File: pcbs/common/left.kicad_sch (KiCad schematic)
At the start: 89 parts, among them J2 TRS

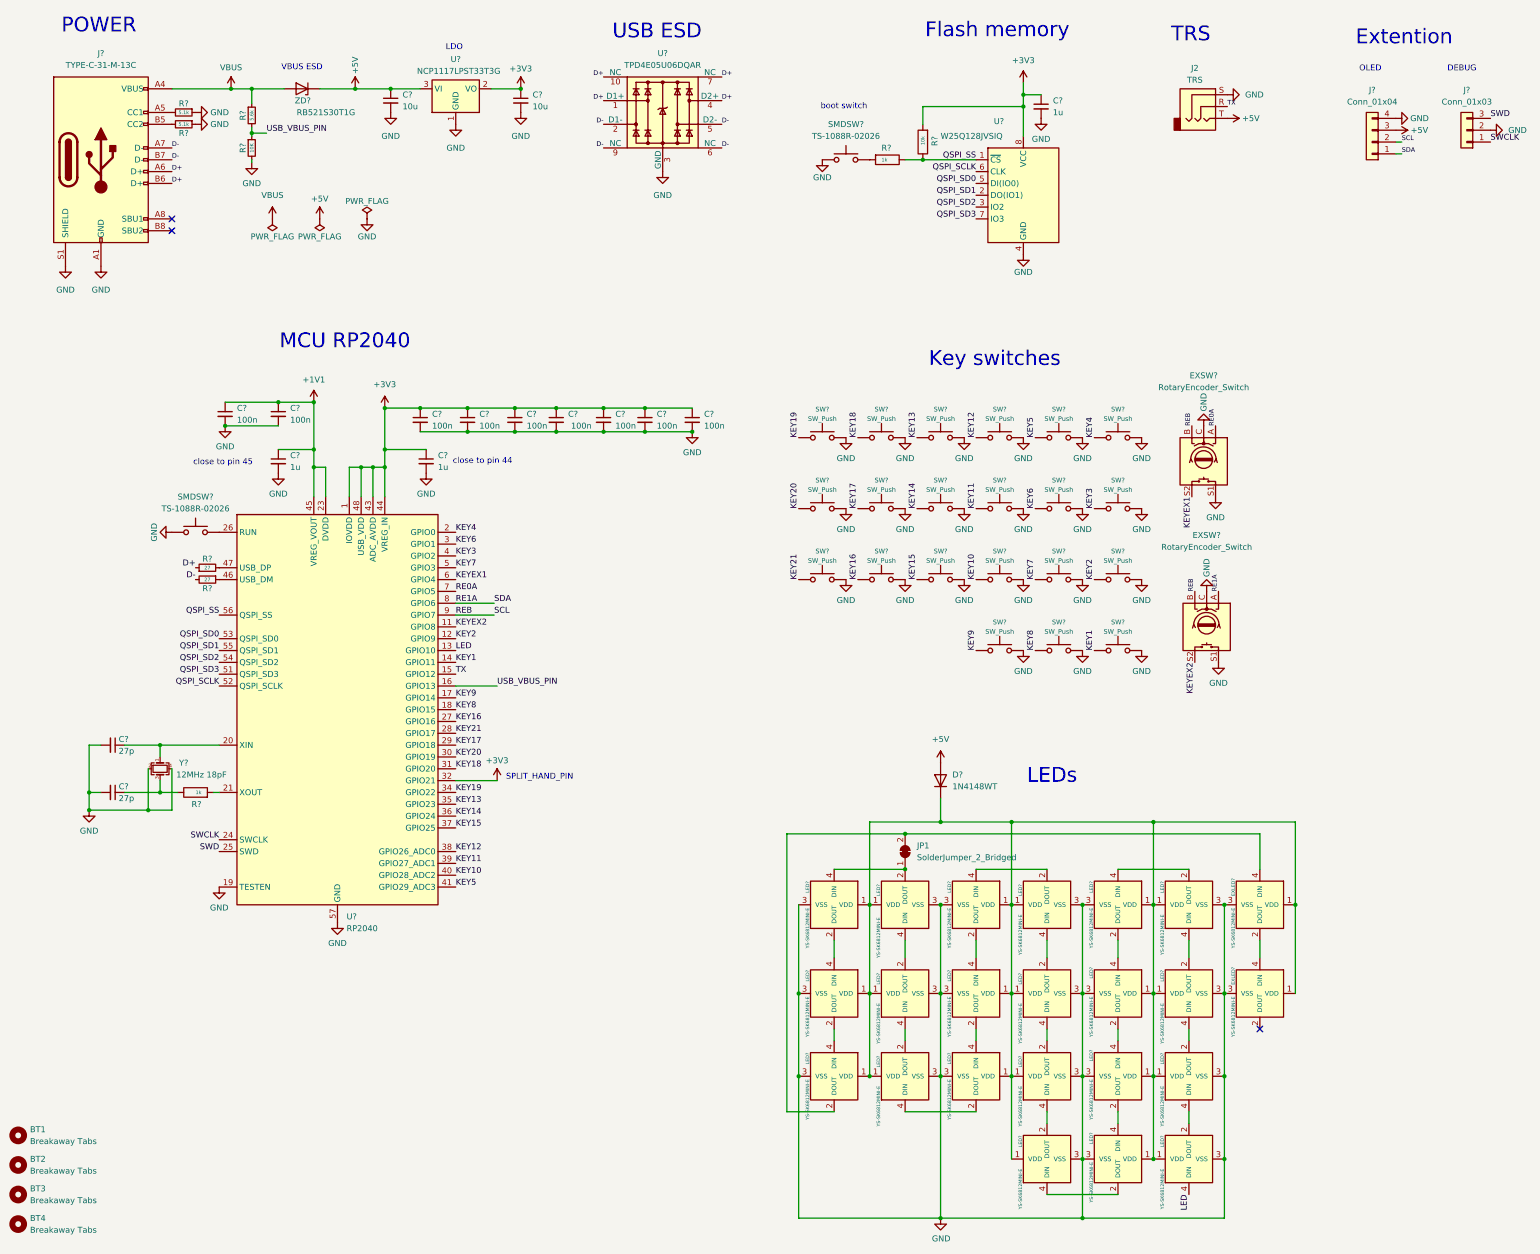
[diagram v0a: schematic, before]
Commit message: Add USB C port to replace TRS jack
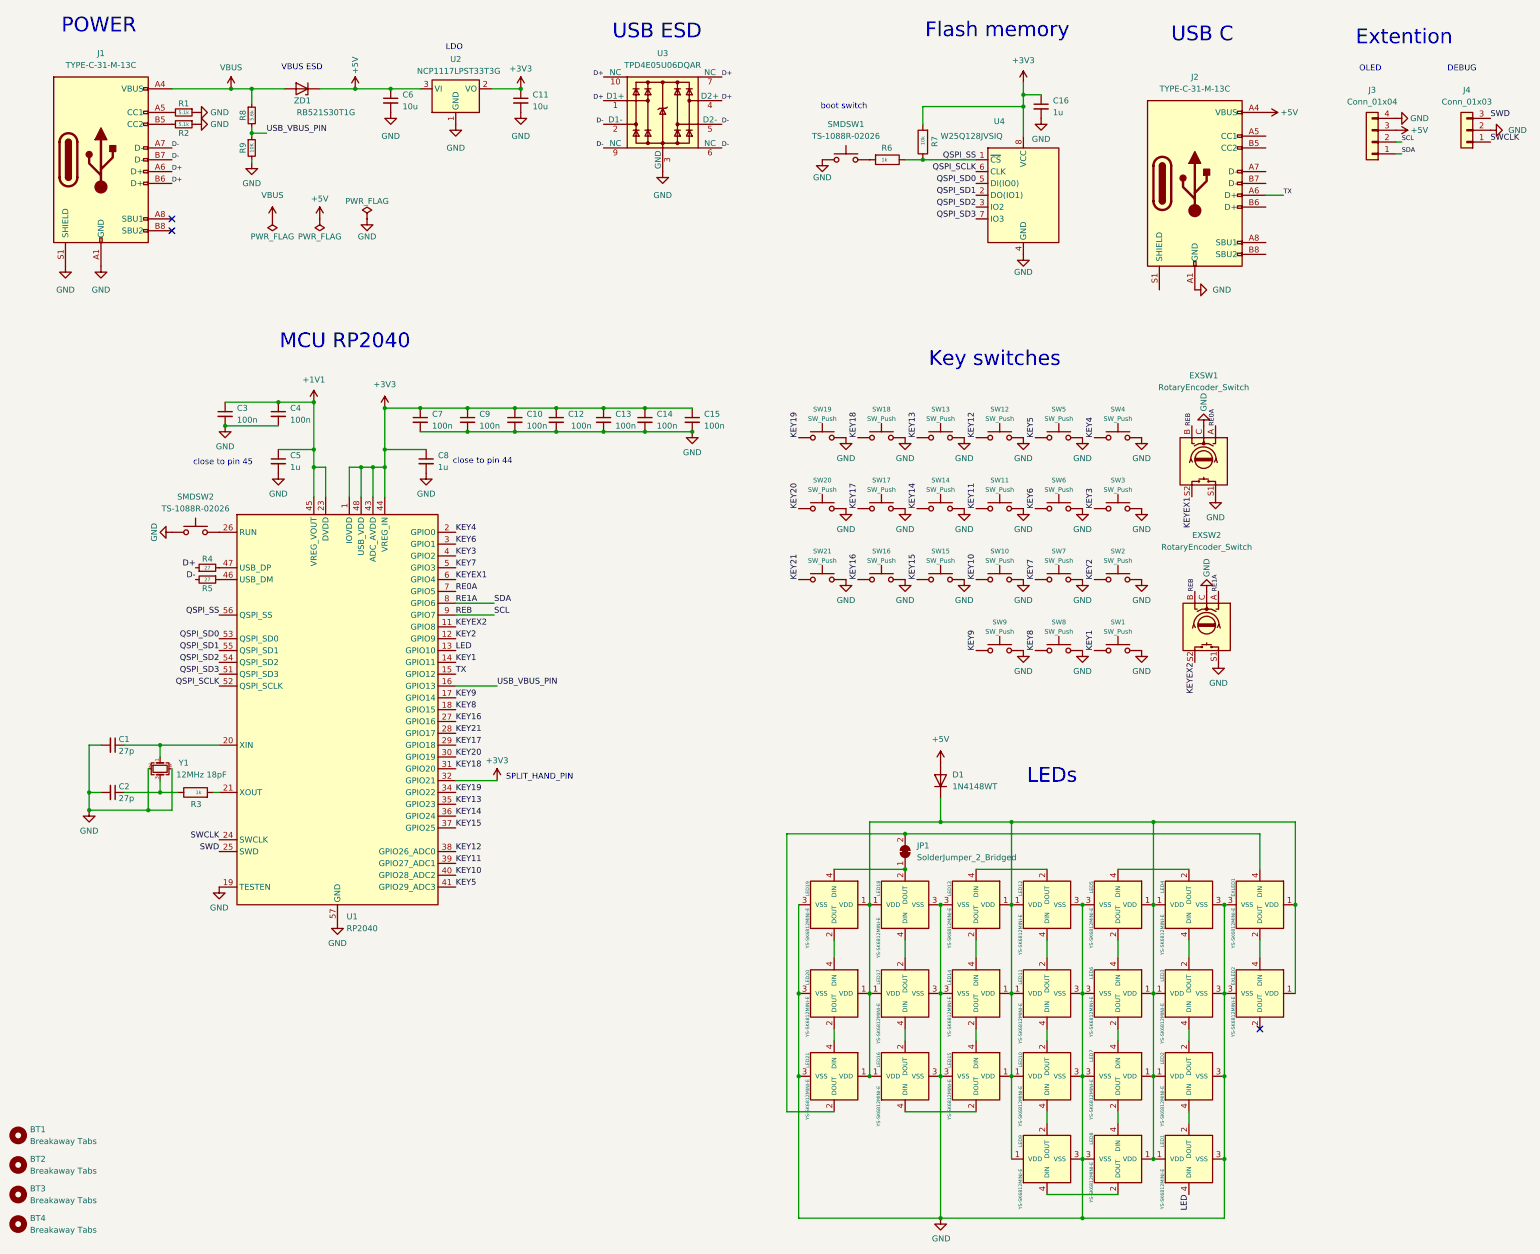
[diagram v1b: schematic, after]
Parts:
- removed J2: TRS, kbd_local:PJ-398A-5A_PJ-399B-6A, symbol Connector_Audio:AudioJack3
- added J2: TYPE-C-31-M-13C, kbd:TYPE-C-31-M-13C, symbol Connector:USB_C_Receptacle_USB2.0
- gave numbers to parts that had none: 83
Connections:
- net +5V: now also J2.A4 (VBUS), J2.A9 (VBUS), J2.B4 (VBUS), J2.B9 (VBUS)
- net GND: now also J2.A1 (GND), J2.A12 (GND), J2.B1 (GND), J2.B12 (GND)
- net TX: now also J2.A6 (D+)
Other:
- note added: "USB C"
- note removed: "TRS"

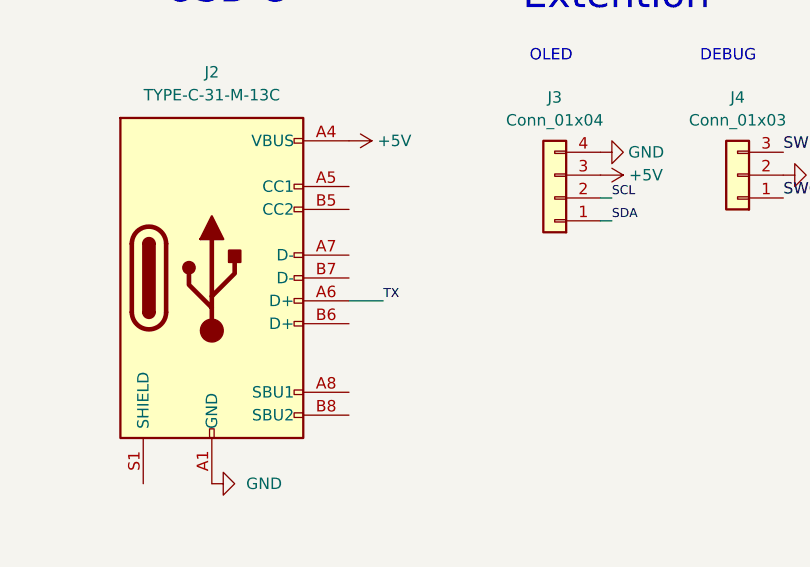
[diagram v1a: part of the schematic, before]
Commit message: Fix some connections
Also connect the other USB D+ pin to the controller.
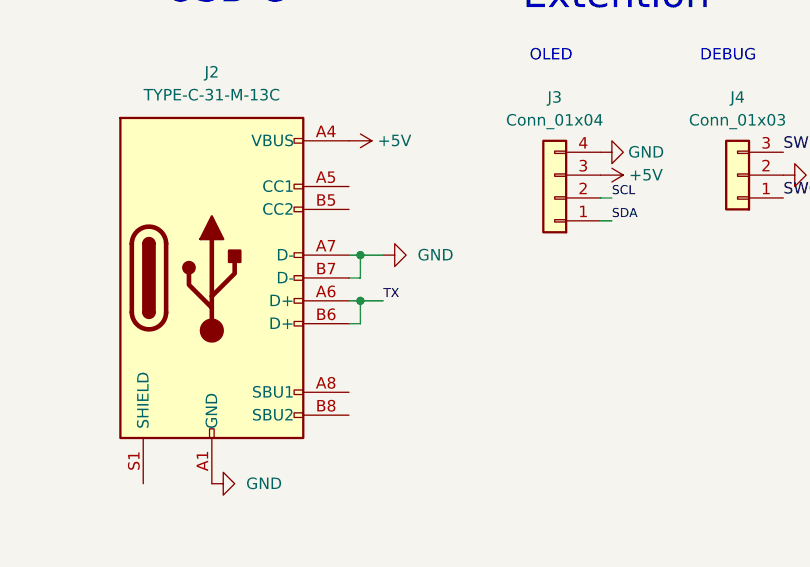
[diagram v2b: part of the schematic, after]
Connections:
- net GND: now also J2.A7 (D-), J2.B7 (D-)
- net TX: now also J2.B6 (D+)
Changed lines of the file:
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@@
 	)
 	(junction
+		(at 287.02 50.8)
+		(diameter 0)
+		(color 0 0 0 0)
+	)
+	(junction
 		(at 81.28 100.33)
 		(diameter 0)
@@
 	)
 	(junction
+		(at 287.02 55.88)
+		(diameter 0)
+		(color 0 0 0 0)
+	)
+	(junction
 		(at 200.66 227.33)
 		(diameter 0)
@@
 	(wire
 		(pts
+			(xy 285.75 50.8) (xy 287.02 50.8)
+		)
+		(stroke
+			(width 0)
+			(type default)
+		)
+	)
+	(wire
+		(pts
 			(xy 233.68 36.83) (xy 233.68 43.18)
 		)
@@
 	(wire
 		(pts
+			(xy 287.02 55.88) (xy 289.56 55.88)
+		)
+		(stroke
+			(width 0)
+			(type default)
+		)
+	)
+	(wire
+		(pts
 			(xy 81.28 110.49) (xy 81.28 114.3)
 		)
@@
 	(wire
 		(pts
+			(xy 285.75 58.42) (xy 287.02 58.42)
+		)
+		(stroke
+			(width 0)
+			(type default)
+		)
+	)
+	(wire
+		(pts
 			(xy 182.88 193.04) (xy 182.88 252.73)
 		)
@@
 	(wire
 		(pts
+			(xy 287.02 50.8) (xy 289.56 50.8)
+		)
+		(stroke
+			(width 0)
+			(type default)
+		)
+	)
+	(wire
+		(pts
 			(xy 261.62 190.5) (xy 261.62 208.28)
 		)
@@
 	(wire
 		(pts
+			(xy 287.02 58.42) (xy 287.02 55.88)
+		)
+		(stroke
+			(width 0)
+			(type default)
+		)
+	)
+	(wire
+		(pts
 			(xy 284.48 215.9) (xy 284.48 219.71)
 		)
@@
 	(wire
 		(pts
+			(xy 287.02 53.34) (xy 287.02 50.8)
+		)
+		(stroke
+			(width 0)
+			(type default)
+		)
+	)
+	(wire
+		(pts
 			(xy 111.76 146.05) (xy 120.015 146.05)
 		)
@@
 	(wire
 		(pts
-			(xy 285.75 55.88) (xy 289.56 55.88)
+			(xy 285.75 55.88) (xy 287.02 55.88)
 		)
 		(stroke
@@
 	(wire
 		(pts
+			(xy 285.75 53.34) (xy 287.02 53.34)
+		)
+		(stroke
+			(width 0)
+			(type default)
+		)
+	)
+	(wire
+		(pts
 			(xy 284.48 193.04) (xy 284.48 200.66)
 		)
@@
 					(unit 1)
 				)
+			)
+		)
+	)
+	(symbol
+		(lib_id "power:GND")
+		(at 289.56 50.8 90)
+		(unit 1)
+		(exclude_from_sim no)
+		(in_bom yes)
+		(on_board yes)
+		(dnp no)
+		(property "Reference" "#PWR74"
+			(at 295.91 50.8 0)
+			(effects
+				(font
+					(size 1.27 1.27)
+				)
+				(hide yes)
+			)
+		)
+		(property "Value" "GND"
+			(at 293.37 50.8 90)
+			(effects
+				(font
+					(size 1.27 1.27)
+				)
+				(justify right)
+			)
+		)
+		(property "Footprint" ""
+			(at 289.56 50.8 0)
+			(effects
+				(font
+					(size 1.27 1.27)
+				)
+				(hide yes)
+			)
+		)
+		(property "Datasheet" ""
+			(at 289.56 50.8 0)
+			(effects
+				(font
+					(size 1.27 1.27)
+				)
+				(hide yes)
+			)
+		)
+		(property "Description" ""
+			(at 289.56 50.8 0)
+			(effects
+				(font
+					(size 1.27 1.27)
+				)
+				(hide yes)
+			)
+		)
+		(pin "1"
+		)
+		(instances
+			(project "corne-cherry"
+				(path "/4cc5d416-57f5-4147-8183-e03ae6b1198a/089db7cd-2934-428b-a62a-55e0735649ba"
+					(reference "#PWR74")
+					(unit 1)
+				)
